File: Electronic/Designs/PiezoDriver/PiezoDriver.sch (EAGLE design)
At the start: 2 parts

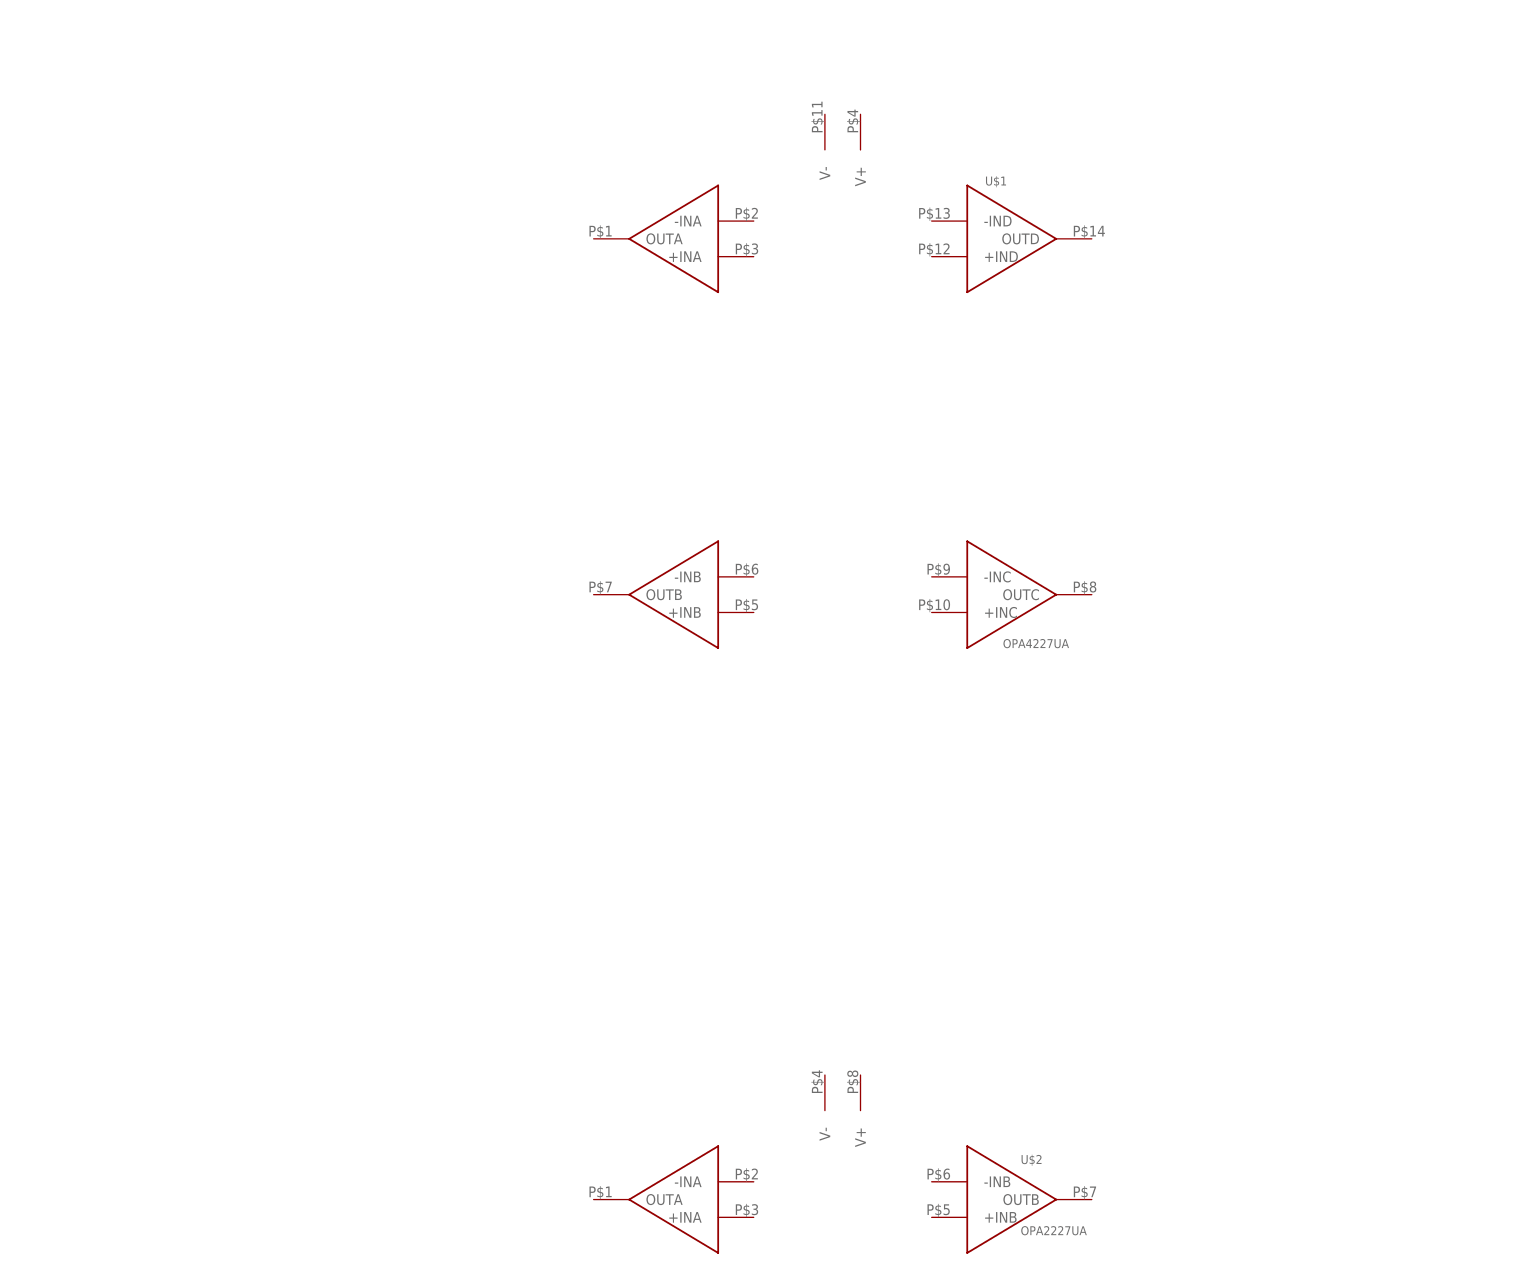
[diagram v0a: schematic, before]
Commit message: Added piezo driver
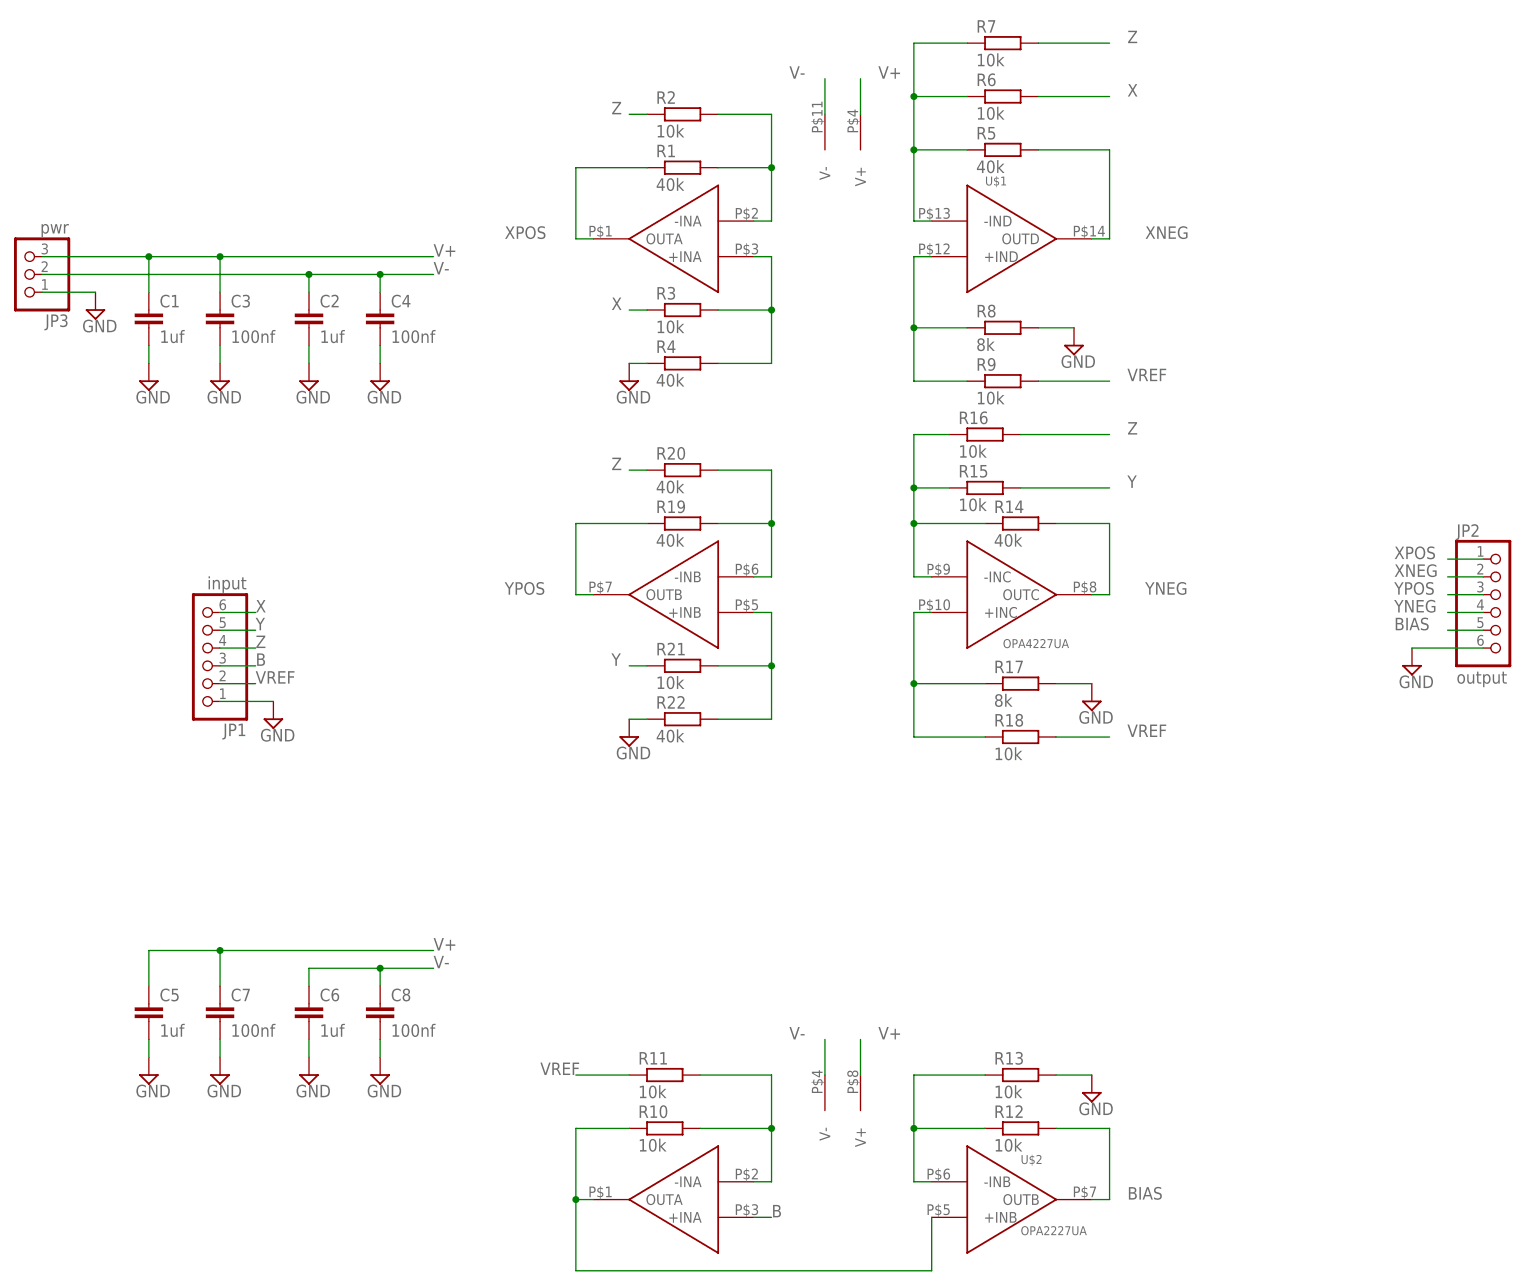
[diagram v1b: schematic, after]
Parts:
- added C1, C2, C5, C6: 1uf, resistor:C-EUC0603
- added C3, C4, C7, C8: 100nf, resistor:C-EUC0603
- added JP1: input, pinhead:PINHD-1X6
- added JP2: output, pinhead:PINHD-1X6
- added JP3: pwr, pinhead:PINHD-1X3
- added R1, R14, R19, R20, R22, R4, R5: 40k, resistor:R-EU_R0603
- added R10, R11, R12, R13, R15, R16, R18, R2, R21, R3, R6, R7, R9: 10k, resistor:R-EU_R0603
- added R17, R8: 8k, resistor:R-EU_R0603
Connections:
- new net B: JP1.3, U$2.+INA
- new net BIAS: JP2.5, R12.2, U$2.OUTB
- new net GND: C1.2, C2.2, C3.2, C4.2, C5.2, C6.2, C7.2, C8.2, JP1.1, JP2.6, JP3.1, R13.2, R17.2, R22.1, R4.1, R8.2
- new net N$1: R1.2, R2.2, U$1.-INA
- new net N$10: R12.1, R13.1, U$2.-INB
- new net N$12: R17.1, R18.1, U$1.+INC
- new net N$13: R21.2, R22.2, U$1.+INB
- new net N$2: R19.2, R20.2, U$1.-INB
- new net N$3: R3.2, R4.2, U$1.+INA
- new net N$4: R14.1, R15.1, R16.1, U$1.-INC
- new net N$5: R5.1, R6.1, R7.1, U$1.-IND
- new net N$6: R8.1, R9.1, U$1.+IND
- new net N$7: R10.1, U$2.+INB, U$2.OUTA
- new net N$8: R10.2, R11.2, U$2.-INA
- new net V+: C1.1, C3.1, C5.1, C7.1, JP3.3, U$1.V+, U$2.V+
- new net V-: C2.1, C4.1, C6.1, C8.1, JP3.2, U$1.V-, U$2.V-
- new net VREF: JP1.2, R11.1, R18.2, R9.2
- new net X: JP1.6, R3.1, R6.2
- new net XNEG: JP2.2, R5.2, U$1.OUTD
- new net XPOS: JP2.1, R1.1, U$1.OUTA
- new net Y: JP1.5, R15.2, R21.1
- new net YNEG: JP2.4, R14.2, U$1.OUTC
- new net YPOS: JP2.3, R19.1, U$1.OUTB
- new net Z: JP1.4, R16.2, R2.1, R20.1, R7.2

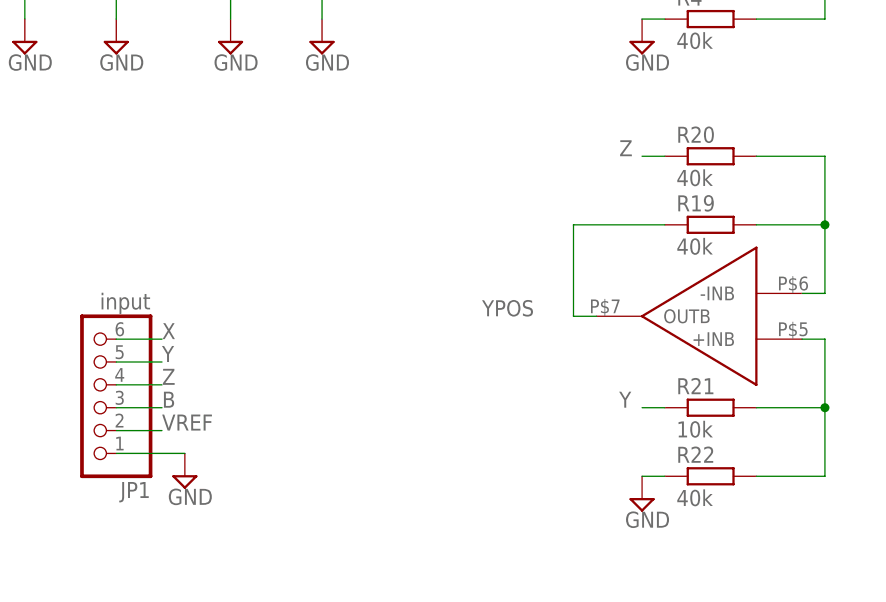
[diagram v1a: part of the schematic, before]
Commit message: Added to Piezo Driver Board
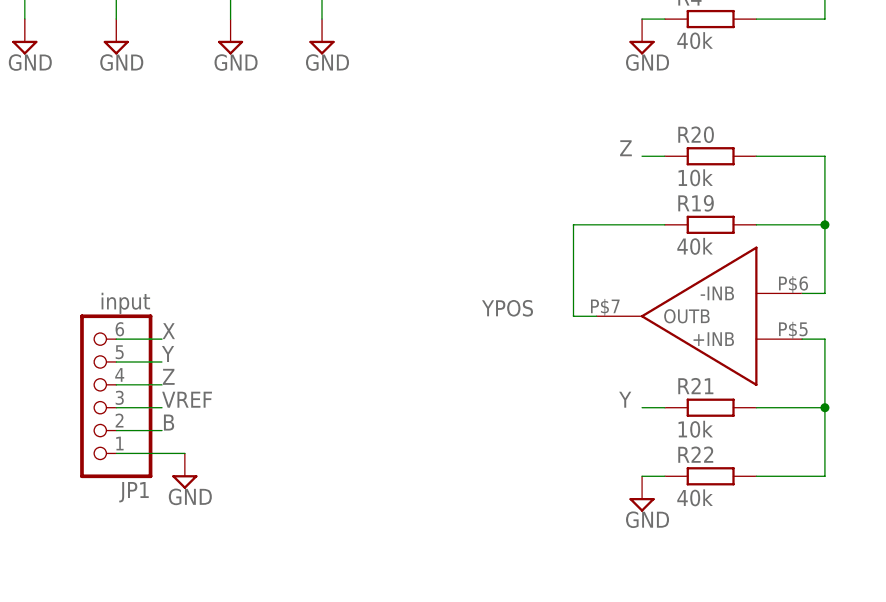
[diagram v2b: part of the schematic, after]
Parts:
- R20: value 40k -> 10k
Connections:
- net B: now also JP1.2; no longer JP1.3
- net VREF: now also JP1.3; no longer JP1.2
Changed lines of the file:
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@@
 <part name="SUPPLY4" library="supply2" deviceset="GND" device=""/>
 <part name="R19" library="resistor" deviceset="R-EU_" device="R0603" value="40k"/>
-<part name="R20" library="resistor" deviceset="R-EU_" device="R0603" value="40k"/>
+<part name="R20" library="resistor" deviceset="R-EU_" device="R0603" value="10k"/>
 <part name="R21" library="resistor" deviceset="R-EU_" device="R0603" value="10k"/>
 <part name="R22" library="resistor" deviceset="R-EU_" device="R0603" value="40k"/>
@@
 </segment>
 <segment>
-<wire x1="-12.7" y1="30.48" x2="-7.62" y2="30.48" width="0.1524" layer="91"/>
-<label x="-7.62" y="30.48" size="1.778" layer="95"/>
-<pinref part="JP1" gate="A" pin="2"/>
-</segment>
-<segment>
 <pinref part="R18" gate="G$1" pin="2"/>
 <wire x1="106.68" y1="22.86" x2="114.3" y2="22.86" width="0.1524" layer="91"/>
 <label x="116.84" y="22.86" size="1.778" layer="95"/>
+</segment>
+<segment>
+<wire x1="-12.7" y1="33.02" x2="-7.62" y2="33.02" width="0.1524" layer="91"/>
+<label x="-7.62" y="33.02" size="1.778" layer="95"/>
+<pinref part="JP1" gate="A" pin="3"/>
 </segment>
 </net>
@@
 </segment>
 <segment>
-<wire x1="-12.7" y1="33.02" x2="-7.62" y2="33.02" width="0.1524" layer="91"/>
-<label x="-7.62" y="33.02" size="1.778" layer="95"/>
-<pinref part="JP1" gate="A" pin="3"/>
-</segment>
-</net>
+<wire x1="-12.7" y1="30.48" x2="-7.62" y2="30.48" width="0.1524" layer="91"/>
+<label x="-7.62" y="30.48" size="1.778" layer="95"/>
+<pinref part="JP1" gate="A" pin="2"/>
+</segment>
+</net>
